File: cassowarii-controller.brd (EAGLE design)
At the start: 36.5 x 26.7 mm, 18 parts, among them J1 Power, J2 2-PIN_2MM-H, J3 2-PIN_2MM-H, U1 ATTiny85

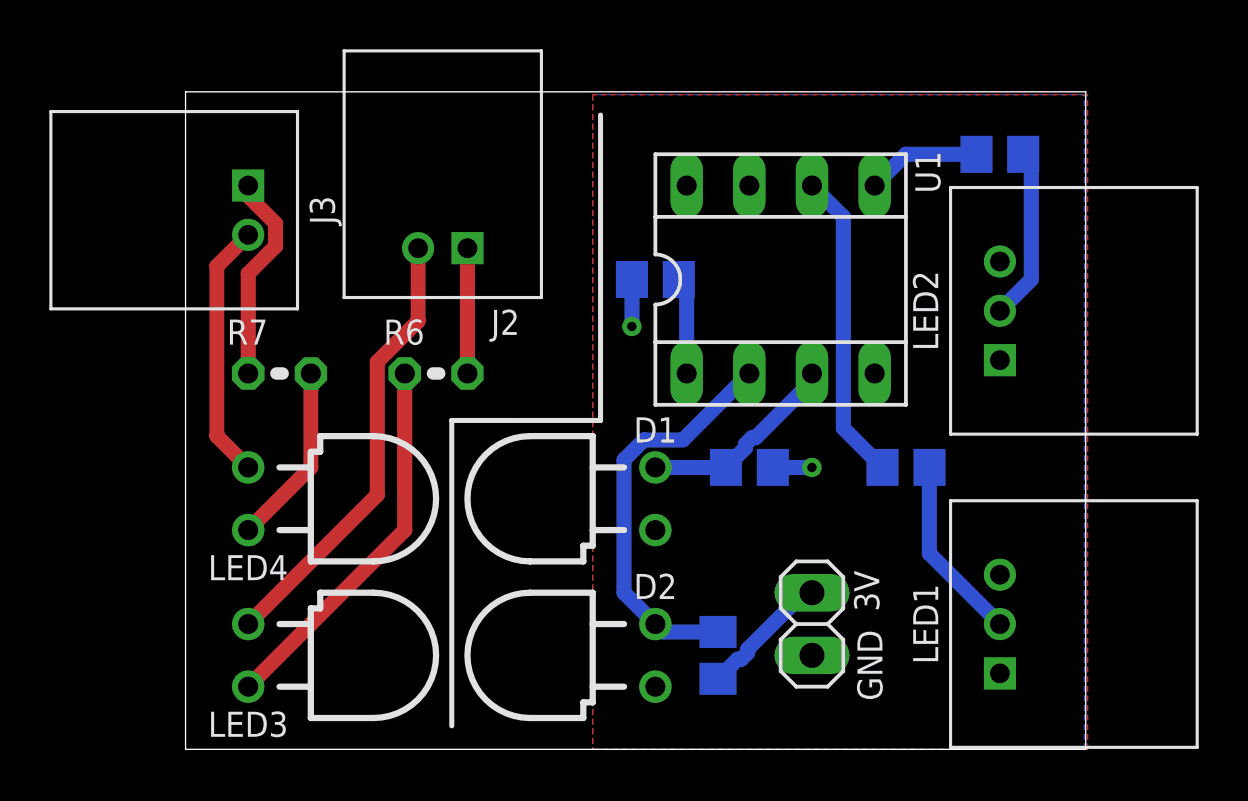
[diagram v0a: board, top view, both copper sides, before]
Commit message: New version of Cassowarii controller with proper optoisolators
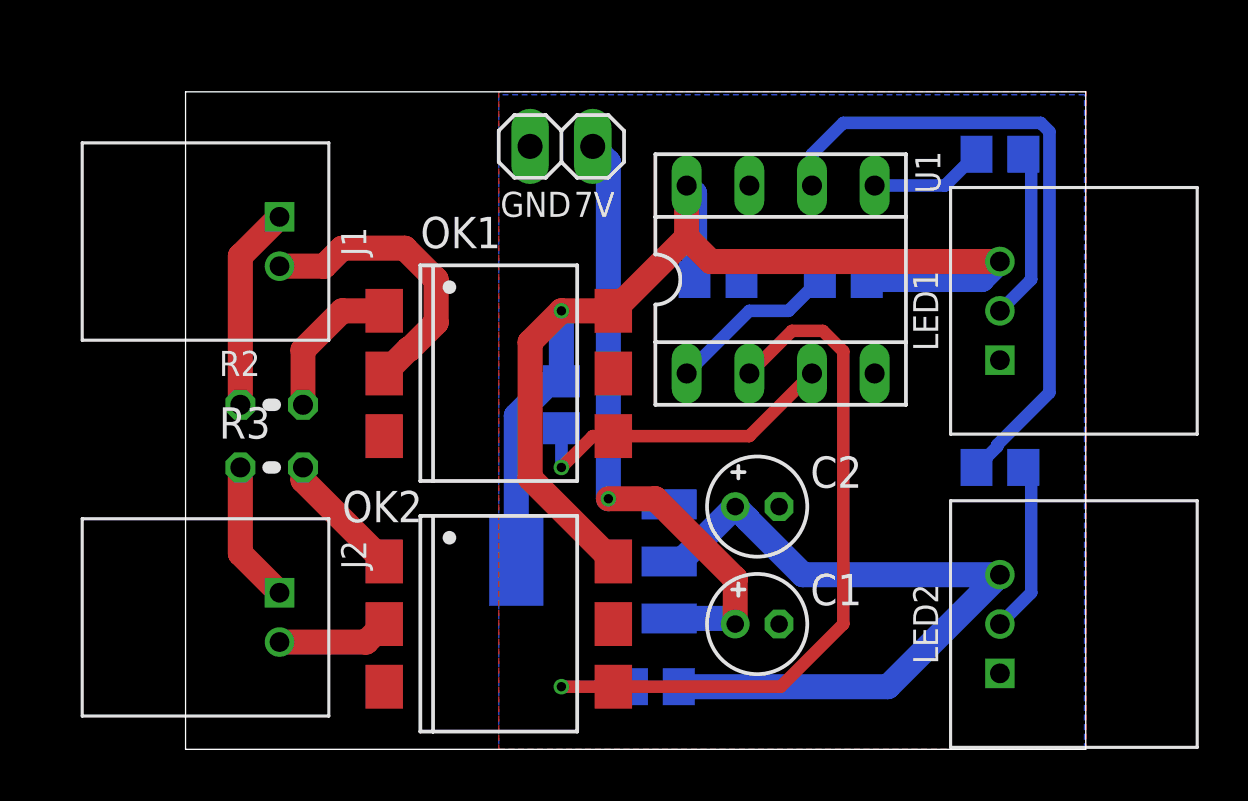
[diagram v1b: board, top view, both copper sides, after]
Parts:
- removed D1, D2: PHOTODIODE, JoshCustom:LED_3MM_HORIZ
- removed J3: 2-PIN_2MM-H, RoboJackets-Connectors:2MM-2-H
- removed LED3, LED4: IR, JoshCustom:LED_3MM_HORIZ
- added C1, C2: 10uF, 10V, resistor:E1,8-4
- added C3: 0.1uF, resistor:C0805
- added JP1: Power, pinhead:1X02
- added OK1, OK2: H11L1MS, optocoupler:DIL6-SMD
- added U2: NCP1117LP, JoshCustom:SOT223
- J1: value Power -> 2-PIN_2MM-H; device pinhead:1X02 -> RoboJackets-Connectors:2MM-2-H
- R1: value 1k -> 10k
- R2, R3: value 470 -> (none); device resistor:R0805 -> resistor:0204V
- R4: value 10k -> 470
- R5: value 1k -> 470
- R6: value 1.5k -> 270; device resistor:0204V -> resistor:R0805
- R7: value 3.3k -> 270; device resistor:0204V -> resistor:R0805
- moved R3 32.1 mm to (3.49, 11.4), flipped to the top, turned to 0 degrees
- moved J1 27.2 mm to (3.81, 21.6)
- moved R2 25.8 mm to (3.49, 14.0), flipped to the top, turned to 0 degrees
- moved R7 19.8 mm to (19.1, 2.54), flipped to the bottom, turned to 180 degrees
- moved R1 16.1 mm to (26.7, 19.1), turned to 180 degrees
- moved J2 15.9 mm to (3.81, 6.35), turned to 270 degrees
- moved R4 14.9 mm to (33.0, 24.1), turned to 180 degrees
- moved LED1 12.7 mm to (33.0, 17.8)
- moved LED2 12.7 mm to (33.0, 5.08)
- moved U$1 12.5 mm to (10.2, 14.0)
- moved R5 10.2 mm to (33.0, 11.4)
- moved R6 5.24 mm to (15.2, 14.0), flipped to the bottom, turned to 90 degrees
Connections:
- removed net N$4: LED3.A, R6.1
- new net N$10: OK2.1, R3.2
- new net N$11: C1.+, JP1.1, U2.3
- net GND: now also C1.-, C2.-, C3.2, JP1.2, OK1.5, OK2.5, U2.1; no longer D1.K, D2.K, J1.2
- net LED1: now also R5.1; no longer R2.1
- net LED2: now also R4.1; no longer R3.1
- net N$1: now also LED1.2, R4.2; no longer LED2.2, R3.2
- net N$2: now also LED2.2, R5.2; no longer LED1.2, R2.2
- net N$3: now also R3.1; no longer R6.2
- net N$5: now also R1.1; no longer R4.1
- net N$6: now also OK2.2; no longer LED3.K
- net N$7: now also J1.1, R2.1; no longer J3.1, R7.1
- net N$8: now also OK1.1, R2.2; no longer LED4.A, R7.2
- net N$9: now also J1.2, OK1.2; no longer J3.2, LED4.K
- net PB3: now also OK2.4, R7.1; no longer D2.A, R1.1
- net PB4: now also OK1.4, R6.1; no longer D1.A, R5.1
- net VCC: now also C2.+, C3.1, OK1.6, OK2.6, R6.2, R7.2, U2.2, U2.4; no longer J1.1, R4.2, R5.2
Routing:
- net VCC: track 8.84 -> 84.8 mm, vias 2 -> 1
- net N$11: track 0.00 -> 25.7 mm, vias 0 -> 1
- net N$4: track 15.3 -> 0.00 mm
- net PB3: track 16.4 -> 31.3 mm, vias 0 -> 1
- net N$6: track 18.1 -> 4.55 mm
- net LED1: track 12.9 -> 26.4 mm
- net N$10: track 0.00 -> 5.17 mm
- net PB4: track 8.20 -> 13.3 mm, vias 0 -> 1
- net N$5: track 3.94 -> 6.98 mm
- net N$9: track 10.5 -> 11.9 mm
- net N$8: track 7.40 -> 6.17 mm
- net N$3: track 5.08 -> 5.74 mm
- added copper zone on layer 1, net GND
- removed copper zone on layer 1, net VCC
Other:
- board text added: "7V"
- board text removed: "3V"

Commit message: Redesign Cassowarii controller to use SOIC ATTiny85
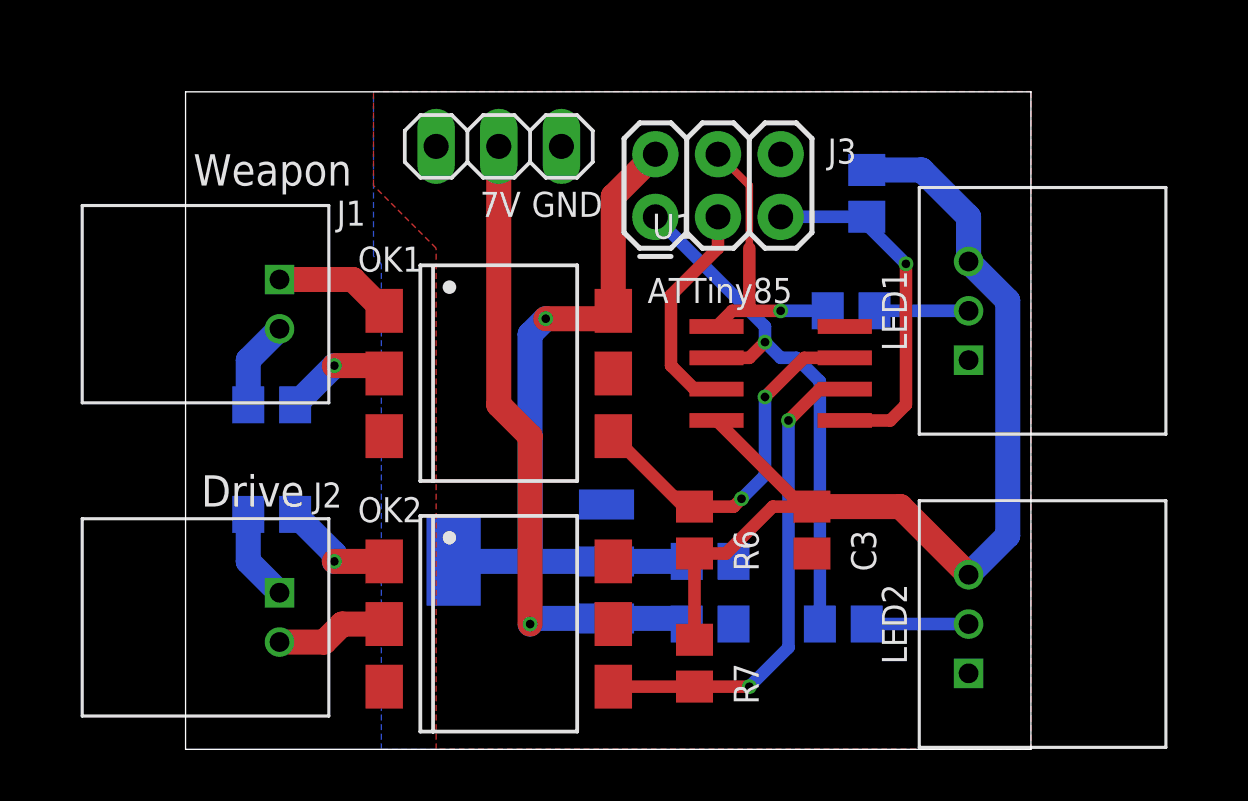
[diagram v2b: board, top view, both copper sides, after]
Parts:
- removed JP1: Power, pinhead:1X02
- added J3: AVR_SPI_PROG_3X2PTH, SparkFun-Connectors:2X3
- added J4: Power, pinhead:1X03
- C1, C2: value 10uF, 10V -> 22uF; device resistor:E1,8-4 -> resistor:C0805
- R2: value (none) -> 3.9k; device resistor:0204V -> resistor:R0805
- R3: value (none) -> 1.5k; device resistor:0204V -> resistor:R0805
- U1: device JoshCustom:SOCKET-08 -> JoshCustom:SOIC8
- U2: value NCP1117LP -> AZ1117IH
- moved C3 10.9 mm to (25.4, 8.89), flipped to the top, turned to 270 degrees
- moved R5 8.98 mm to (26.7, 5.08)
- moved R4 8.76 mm to (27.0, 17.8)
- moved R6 7.41 mm to (20.6, 8.89), flipped to the top, turned to 270 degrees
- moved U1 3.81 mm to (24.1, 15.2), turned to 90 degrees
- moved R1 3.62 mm to (27.6, 22.5), turned to 90 degrees
- moved C2 2.93 mm to (21.3, 7.62), flipped to the bottom, turned to 180 degrees
- moved U$1 2.54 mm to (10.2, 11.4)
- moved U2 2.54 mm to (14.0, 7.62)
- moved J1 2.54 mm to (3.81, 19.1)
- moved R3 1.90 mm to (3.49, 9.53), flipped to the bottom, turned to 180 degrees
- moved C1 1.90 mm to (21.3, 5.08), flipped to the bottom, turned to 180 degrees
- moved R7 1.85 mm to (20.6, 3.49), flipped to the top, turned to 90 degrees
- moved LED1 1.27 mm to (31.8, 17.8)
- moved LED2 1.27 mm to (31.8, 5.08)
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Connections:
- removed net N$11: C1.+, JP1.1, U2.3
- removed net N$8: OK1.1, R2.2
- removed net N$9: J1.2, OK1.2
- new net N$4: J1.2, R2.1
- new net RESET: J3.5, R1.1, U1.1
- new net VIN: C1.1, J4.2, U2.3
- net GND: now also C1.2, C2.2, J3.6, J4.1, J4.3; no longer C1.-, C2.-, JP1.2
- net LED1: now also J3.1
- net LED2: now also J3.4
- net N$5: now also OK1.2, R2.2; no longer R1.1, U1.1
- net N$7: now also OK1.1; no longer R2.1
- net PB2: now also J3.3
- net VCC: now also C2.1, J3.2; no longer C2.+
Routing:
- net VIN: track 0.00 -> 26.4 mm, vias 0 -> 1
- net N$11: track 25.7 -> 0.00 mm, vias 1 -> 0
- net RESET: track 0.00 -> 14.5 mm, vias 0 -> 1
- net VCC: track 84.8 -> 72.1 mm
- net N$9: track 11.9 -> 0.00 mm
- net PB3: track 31.3 -> 19.8 mm, vias 1 -> 2
- net PB2: track 0.00 -> 9.06 mm
- net LED2: track 4.66 -> 11.6 mm, vias 0 -> 1
- net N$8: track 6.17 -> 0.00 mm
- net LED1: track 26.4 -> 21.9 mm, vias 0 -> 1
- net N$4: track 0.00 -> 3.61 mm
- net N$7: track 8.28 -> 4.77 mm
- net N$1: track 7.01 -> 3.81 mm
- net N$2: track 7.20 -> 4.13 mm
- net N$5: track 6.98 -> 4.40 mm, vias 0 -> 1
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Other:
- board size 36.5 x 26.7 mm -> 34.3 x 26.7 mm
- board text added: "Drive"
- board text added: "Isolated Neopixel controller v1 RoboJackets, 2019"
- board text added: "Weapon"
- board text removed: "Isolated Neopixel controller"

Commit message: Fix DRC errors
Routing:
- net VCC: track 72.1 -> 75.5 mm, vias 1 -> 2
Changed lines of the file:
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@@
 <wire x1="31.75" y1="21.59" x2="29.8475" y2="23.4925" width="1.016" layer="16"/>
 <wire x1="29.8475" y1="23.4925" x2="27.6225" y2="23.4925" width="1.016" layer="16"/>
-<wire x1="17.0688" y1="7.62" x2="20.3225" y2="7.62" width="1.016" layer="16"/>
+<wire x1="17.0688" y1="7.62" x2="19.05" y2="7.62" width="1.016" layer="16"/>
+<wire x1="19.05" y1="7.62" x2="20.3225" y2="7.62" width="1.016" layer="16"/>
 <wire x1="10.871" y1="7.62" x2="13.97" y2="7.62" width="1.016" layer="16"/>
 <wire x1="13.97" y1="7.62" x2="17.0688" y2="7.62" width="1.016" layer="16"/>
@@
 <wire x1="21.53" y1="13.335" x2="25.025" y2="9.84" width="0.508" layer="1"/>
 <wire x1="25.025" y1="9.84" x2="25.4" y2="9.84" width="0.508" layer="1"/>
-<wire x1="20.6375" y1="4.4425" x2="20.6375" y2="7.94" width="0.508" layer="1"/>
-<wire x1="20.6375" y1="7.94" x2="21.91" y2="7.94" width="0.508" layer="1"/>
-<wire x1="23.81" y1="9.84" x2="25.4" y2="9.84" width="0.508" layer="1"/>
-<wire x1="21.91" y1="7.94" x2="23.81" y2="9.84" width="0.508" layer="1"/>
-<wire x1="17.0688" y1="7.62" x2="17.345" y2="7.62" width="0" layer="19" extent="1-16"/>
-<wire x1="20.6375" y1="7.94" x2="20.3225" y2="7.62" width="0" layer="19" extent="1-16"/>
+<wire x1="20.6375" y1="4.4425" x2="20.6375" y2="7.94" width="1.016" layer="1"/>
+<wire x1="17.345" y1="7.62" x2="19.05" y2="7.62" width="1.016" layer="1"/>
+<wire x1="19.05" y1="7.62" x2="20.3175" y2="7.62" width="1.016" layer="1"/>
+<wire x1="20.3175" y1="7.62" x2="20.6375" y2="7.94" width="1.016" layer="1"/>
+<wire x1="20.6375" y1="7.94" x2="21.91" y2="7.94" width="1.016" layer="1"/>
+<wire x1="23.81" y1="9.84" x2="25.4" y2="9.84" width="1.016" layer="1"/>
+<wire x1="21.91" y1="7.94" x2="23.81" y2="9.84" width="1.016" layer="1"/>
+<via x="19.05" y="7.62" extent="1-16" drill="0.35"/>
 </signal>
 <signal name="GND">
